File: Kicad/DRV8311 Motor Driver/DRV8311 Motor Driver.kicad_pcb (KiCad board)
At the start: 4 copper layers, 11 x 11 mm, 22 parts, among them J1 B, J2 A, J3 C, U1 DRV8311HRRWR

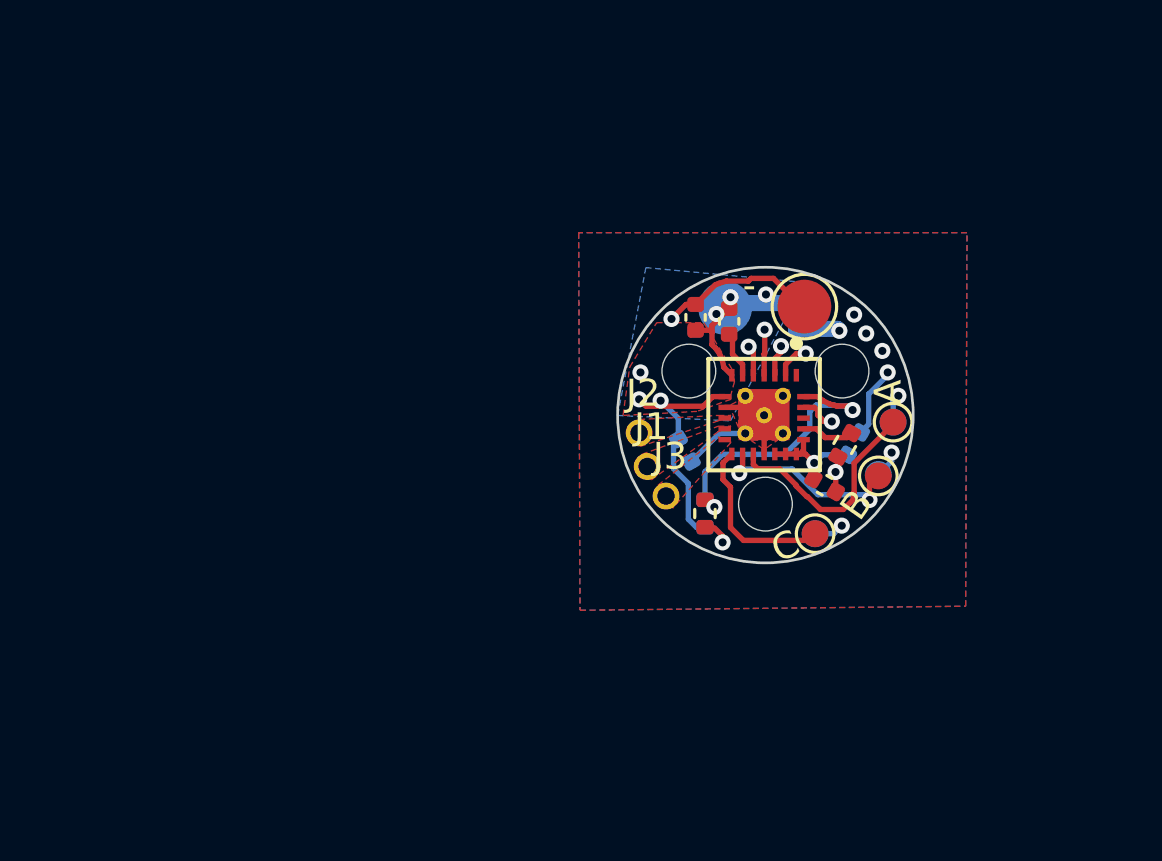
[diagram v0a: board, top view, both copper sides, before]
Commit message: Replaced external connectors
I have keystone smd low profile contacts for the power, and 1.27mm pitch headers for the data pins.
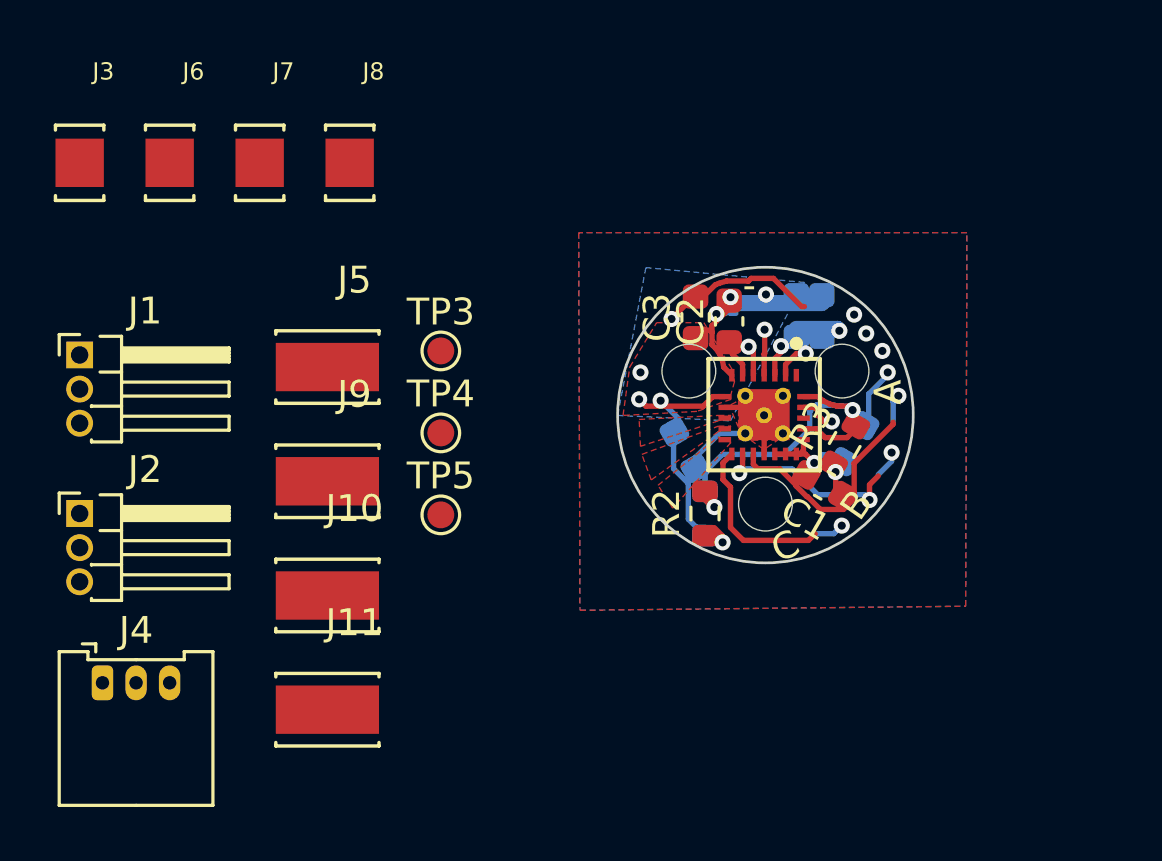
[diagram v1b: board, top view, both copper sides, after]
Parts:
- removed TP1: Power, TestPoint:TestPoint_Pad_D2.0mm
- removed TP2: GND, TestPoint:TestPoint_Pad_D2.0mm
- removed TP6: CSA-C, TestPoint:TestPoint_Pad_D1.0mm
- removed TP7: B, TestPoint:TestPoint_Pad_D1.0mm
- removed TP8: C, TestPoint:TestPoint_Pad_D1.0mm
- added J10: Keystone 6102, 6102:KEYSTONE_6102, F.Cu at (155.0, 107.2)
- added J11: Keystone 6102, 6102:KEYSTONE_6102, F.Cu at (155.0, 111.4)
- added J4: Molex Picoblade, Connector_Molex:Molex_PicoBlade_53048-0310_1x03_P1.25mm_Horizontal, F.Cu at (146.6, 110.4)
- added J5: Keystone 6102, 6102:KEYSTONE_6102, F.Cu at (155.0, 98.7)
- added J6: Keystone 6100, 6100:KEYSTONE_6100, F.Cu at (149.1, 91.0)
- added J7: Keystone 6100, 6100:KEYSTONE_6100, F.Cu at (152.5, 91.0)
- added J8: Keystone 6100, 6100:KEYSTONE_6100, F.Cu at (155.8, 91.0)
- added J9: Keystone 6102, 6102:KEYSTONE_6102, F.Cu at (155.0, 102.9)
- C1, C2, C3, C6, C7: footprint Capacitor_SMD:C_0402_1005Metric -> Capacitor_SMD:C_0603_1608Metric
- C4, C5: value 22uF -> 22uF, 16v; footprint Capacitor_SMD:C_0402_1005Metric -> Capacitor_SMD:C_0603_1608Metric
- J1: value B -> 1.27mm pin header; footprint custom_testpoints:PinHeader_1x01_P1.27mm_Round -> Connector_PinHeader_1.27mm:PinHeader_1x03_P1.27mm_Horizontal
- J2: value A -> 1.27mm pin header; footprint custom_testpoints:PinHeader_1x01_P1.27mm_Round -> Connector_PinHeader_1.27mm:PinHeader_1x03_P1.27mm_Horizontal
- J3: value C -> Keystone 6100; footprint custom_testpoints:PinHeader_1x01_P1.27mm_Round -> 6100:KEYSTONE_6100
- R1, R2, R3: footprint Resistor_SMD:R_0402_1005Metric -> Resistor_SMD:R_0603_1608Metric
- TP3: value CSA-A -> Fault; moved to F.Cu
- TP4: value CSA-B -> GND; moved to F.Cu
- TP5: value A -> 3.3v
- moved J3 25.1 mm to (145.8, 91.0)
- moved J1 21.5 mm to (145.8, 98.2)
- moved J2 21.0 mm to (145.8, 104.1)
- moved TP5 17.2 mm to (159.2, 104.2)
- moved TP4 16.4 mm to (159.2, 101.1), turned to 0 degrees
- moved TP3 15.5 mm to (159.2, 98.0), turned to 0 degrees
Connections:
- C3 pad 2: GND -> GNDPWR
- C4 pad 2: GND -> GNDPWR
- C5 pad 2: GND -> GNDPWR
- C6 pad 2: GND -> GNDPWR
- J3 pad 1: Net-(J3-Pin_1) -> GNDPWR
- TP3 pad 1: Net-(U1-SOA) -> Net-(U1-FAULT_N)
- TP4 pad 1: Net-(U1-SOB) -> GND
- TP5 pad 1: Net-(U1-INHA) -> +3.3V
- U1 pad 1: unconnected-(U1-FAULT_N-Pad1) -> Net-(U1-FAULT_N)
- U1 pad 10: Net-(J2-Pin_1) -> Net-(J4-Pin_3)
- U1 pad 11: Net-(J1-Pin_1) -> Net-(J4-Pin_2)
- U1 pad 12: Net-(J3-Pin_1) -> Net-(J4-Pin_1)
- U1 pad 13: Net-(U1-INHC) -> Net-(J2-Pin_3)
- U1 pad 14: Net-(U1-INHB) -> Net-(J2-Pin_2)
- U1 pad 15: Net-(U1-INHA) -> Net-(J2-Pin_1)
- U1 pad 25: GND -> GNDPWR
- U1 pad 3: Net-(U1-SOC) -> Net-(J1-Pin_1)
- U1 pad 4: Net-(U1-SOB) -> Net-(J1-Pin_2)
- U1 pad 5: Net-(U1-SOA) -> Net-(J1-Pin_3)
- U1 pad 9: GND -> GNDPWR
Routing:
- net (no net): track 0.00 -> 36.2 mm, vias 0 -> 2
- net Net-(U1-SOB): track 14.0 -> 0.00 mm, vias 2 -> 0
- net Net-(J1-Pin_2): track 0.00 -> 14.0 mm, vias 0 -> 2
- net Net-(U1-SOA): track 13.9 -> 0.00 mm, vias 2 -> 0
- net Net-(U1-SOC): track 13.8 -> 0.00 mm, vias 2 -> 0
- net Net-(U1-INHA): track 8.46 -> 0.00 mm
- net Net-(U1-INHB): track 7.18 -> 0.00 mm, vias 2 -> 0
- net Net-(J2-Pin_2): track 0.00 -> 7.18 mm, vias 0 -> 2
- net Net-(U1-INHC): track 6.44 -> 0.00 mm
- net Net-(J2-Pin_3): track 0.00 -> 6.44 mm
- net GND: track 17.6 -> 11.6 mm, vias 8 -> 7
- net GNDPWR: track 0.00 -> 5.97 mm, vias 0 -> 1
- net Net-(J1-Pin_1): vias 0 -> 2
- added copper zone on F.Cu, net Net-(J4-Pin_1)
- removed copper zone on F.Cu, net Net-(J3-Pin_1)

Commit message: Finished basic layout for motor driver card
The power connectors as of now have no way of contacting adjacent cards. The layout will need some tuning, but I think the components for the most part can stay in the same place.
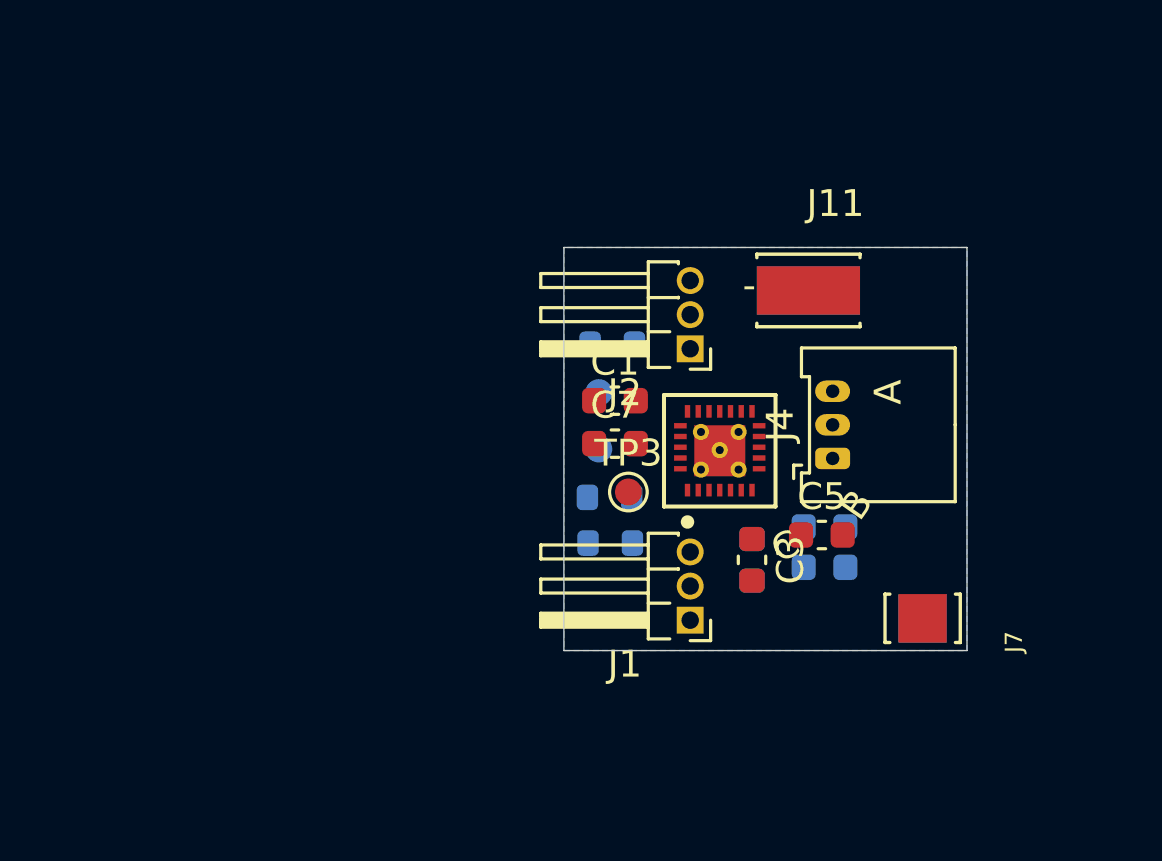
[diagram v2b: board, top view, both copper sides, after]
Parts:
- removed J10, J9: Keystone 6102, 6102:KEYSTONE_6102
- removed J6, J8: Keystone 6100, 6100:KEYSTONE_6100
- C2, J3, J5, R2, R3, TP4, TP5: moved to B.Cu
- C5, C7: moved to F.Cu
- moved J3 35.7 mm to (177.2, 108.0), turned to 90 degrees
- moved J7 29.9 mm to (177.2, 108.0), turned to -90 degrees
- moved J4 28.4 mm to (173.8, 102.0), turned to 90 degrees
- moved J1 24.8 mm to (168.5, 108.1), turned to 180 degrees
- moved J11 23.7 mm to (172.9, 95.8)
- moved J2 23.5 mm to (168.5, 98.0), turned to 180 degrees
- moved J5 18.1 mm to (172.9, 95.8), turned to 180 degrees
- moved R3 9.43 mm to (165.6, 97.8), turned to 0 degrees
- moved C3 9.27 mm to (170.8, 105.8), turned to -90 degrees
- moved C2 8.92 mm to (170.8, 105.8), turned to -90 degrees
- moved C7 8.90 mm to (165.7, 101.5), turned to 0 degrees
- moved TP3 8.73 mm to (166.2, 103.3)
- moved C1 8.41 mm to (165.7, 99.9), turned to 0 degrees
- moved C5 8.15 mm to (173.4, 104.9), turned to 0 degrees
- moved C4 7.92 mm to (173.5, 104.6), turned to 0 degrees
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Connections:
- U1 pad 10: Net-(J4-Pin_3) -> Net-(J4-Pin_1)
- U1 pad 12: Net-(J4-Pin_1) -> Net-(J4-Pin_3)
- U1 pad 3: Net-(J1-Pin_1) -> Net-(J1-Pin_3)
- U1 pad 5: Net-(J1-Pin_3) -> Net-(J1-Pin_1)
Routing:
- net (no net): track 36.2 -> 0.00 mm, vias 2 -> 0
- net VDD: track 19.0 -> 0.00 mm, vias 6 -> 0
- net Net-(J1-Pin_2): track 14.0 -> 0.00 mm, vias 2 -> 0
- net +3.3V: track 11.7 -> 0.00 mm, vias 3 -> 0
- net GND: track 11.6 -> 0.00 mm, vias 7 -> 0
- net Net-(U1-SLEEP_N): track 11.0 -> 0.00 mm, vias 2 -> 0
- net Net-(J2-Pin_2): track 7.18 -> 0.00 mm, vias 2 -> 0
- net Net-(J2-Pin_3): track 6.44 -> 0.00 mm
- net GNDPWR: track 5.97 -> 0.00 mm, vias 1 -> 0
- net Net-(U1-GAIN): track 1.99 -> 0.00 mm
- net Net-(U1-CP): track 1.73 -> 0.00 mm
- net Net-(J1-Pin_1): vias 2 -> 0
- removed copper zone on B.Cu, net GND
- removed copper zone on F.Cu, net GND
- removed copper zone on In1.Cu, net GND
- removed copper zone on F.Cu, net Net-(J1-Pin_1)
- removed copper zone on F.Cu, net Net-(J2-Pin_1)
- removed copper zone on F.Cu, net Net-(J4-Pin_1)
- removed copper zone on F.Cu, net VDD
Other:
- board size 11 x 11 mm -> 15 x 15 mm
- board text removed: "----"
- board text removed: "08/17/2024"
- board text removed: "1"
- board text removed: "1 of 1"
- board text removed: "2"
- board text removed: "8:1"
- board text removed: "APPROVED"
- board text removed: "ASHER"
- board text removed: "BREAK ALL SHARP EDGES AND REMOVE BURRS"
- board text removed: "Bottom Motor view"
- board text removed: "CHECKED"
- board text removed: "DATE"
- board text removed: "DO NOT SCALE DRAWING"
- board text removed: "DRAWN"
- board text removed: "DWG NO."
- board text removed: "FINISH"
- board text removed: "MATERIAL"
- board text removed: "NAME"
- board text removed: "REV."
- board text removed: "SCALE"
- board text removed: "SHEET"
- board text removed: "SIZE"
- board text removed: "SURFACE FINISH"
- board text removed: "THIRD ANGLE PROJECTION"
- board text removed: "TITLE"
- board text removed: "UNLESS OTHERWISE SPECIFIED, DIMENSIONS ARE IN MILLIMETERS"
- board text removed: "WEIGHT"

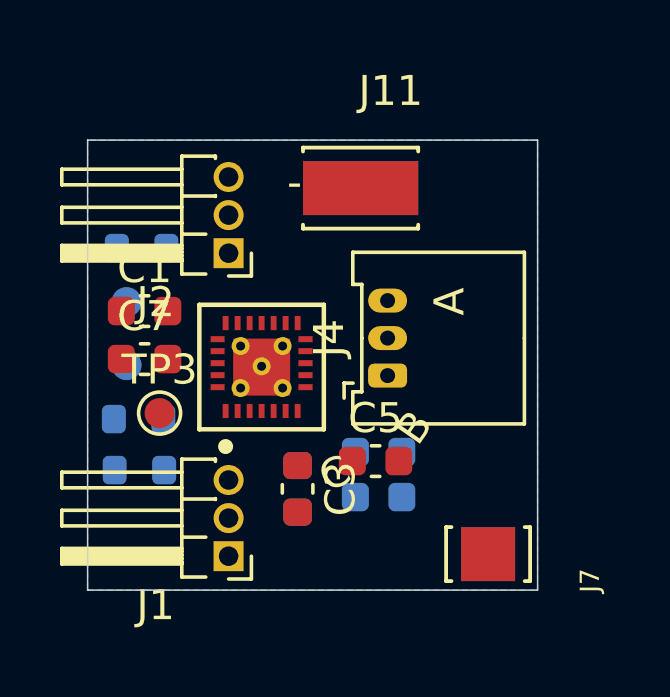
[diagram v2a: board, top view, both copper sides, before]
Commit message: Re-arranged components for better mating
The power connectors now should make contact. The difficulty will be getting them in, because they are supposed to go forward and I'm causing the connectors to slide in sidewards.
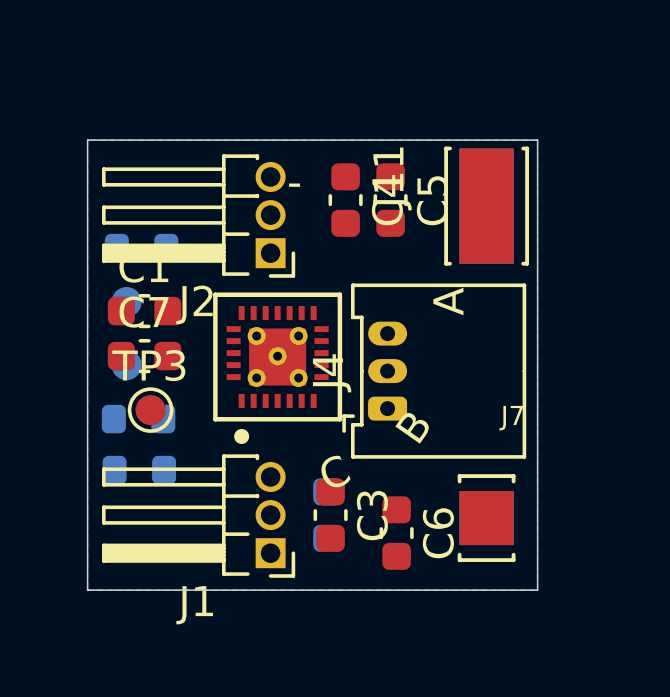
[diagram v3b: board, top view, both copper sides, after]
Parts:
- C4, C6: moved to F.Cu
- moved C5 8.71 mm to (173.9, 96.2), turned to -90 degrees
- moved C4 8.47 mm to (172.4, 96.2), turned to -90 degrees
- moved J11 4.24 mm to (177.1, 96.4), turned to 90 degrees
- moved J5 4.24 mm to (177.1, 96.4), turned to -90 degrees
- moved C3 1.41 mm to (171.9, 106.7)
- moved J1 1.40 mm to (169.9, 108.0)
- moved J2 1.40 mm to (169.9, 98.0)
- moved C6 1.34 mm to (174.1, 107.3), turned to -90 degrees
- moved C2 1.33 mm to (171.8, 106.7)
- moved J3 1.20 mm to (177.1, 106.8), turned to 180 degrees
- moved J7 1.20 mm to (177.1, 106.8), turned to 0 degrees
- moved J4 1.10 mm to (173.8, 103.2)
- moved U1 0.63 mm to (170.1, 101.4)
- moved TP3 0.32 mm to (165.9, 103.2)
- moved C7 0.10 mm to (165.7, 101.4)

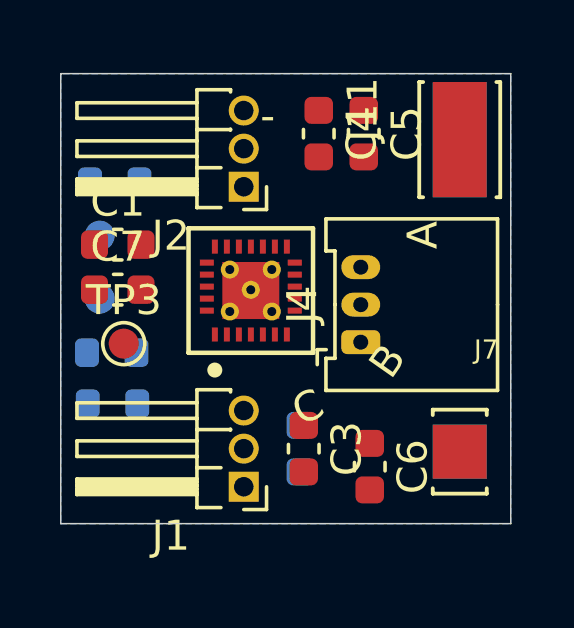
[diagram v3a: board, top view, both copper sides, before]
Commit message: Finished basic routing
I still need to optimize it, and work out how to improve conductivity and thermal properties
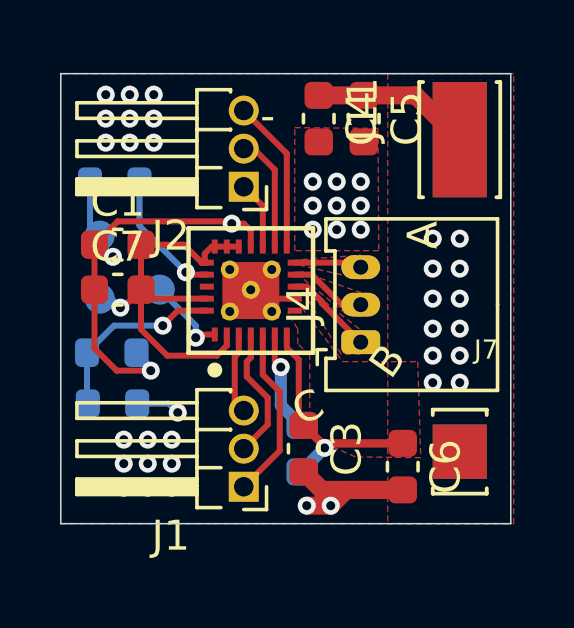
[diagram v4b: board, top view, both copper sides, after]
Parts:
- TP3: moved to B.Cu
- moved TP3 2.16 mm to (167.1, 101.4), turned to 180 degrees
- moved C6 1.10 mm to (175.2, 107.3)
- moved C4 0.50 mm to (172.4, 95.7)
- moved C5 0.50 mm to (173.9, 95.7)
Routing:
- net VDD: track 0.00 -> 21.0 mm, vias 0 -> 14
- net GND: track 0.00 -> 16.2 mm, vias 0 -> 3
- net +3.3V: track 0.00 -> 14.6 mm, vias 0 -> 1
- net GNDPWR: track 0.00 -> 8.54 mm, vias 0 -> 29
- net Net-(U1-SLEEP_N): track 0.00 -> 6.29 mm, vias 0 -> 1
- net Net-(J1-Pin_1): track 0.00 -> 5.81 mm
- net Net-(J2-Pin_3): track 0.00 -> 5.13 mm
- net Net-(J1-Pin_2): track 0.00 -> 4.48 mm
- net Net-(U1-GAIN): track 0.00 -> 4.29 mm, vias 0 -> 1
- net Net-(J2-Pin_2): track 0.00 -> 3.89 mm
- net Net-(U1-CP): track 0.00 -> 3.39 mm, vias 0 -> 1
- net Net-(J4-Pin_1): track 0.00 -> 3.00 mm
- net Net-(U1-FAULT_N): track 0.00 -> 2.78 mm, vias 0 -> 1
- net Net-(J1-Pin_3): track 0.00 -> 2.72 mm
- net Net-(J4-Pin_2): track 0.00 -> 2.61 mm
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- added copper zone on B.Cu, net GNDPWR
- added copper zone on F.Cu, net GNDPWR
- added copper zone on In2.Cu, net GNDPWR
- added copper zone on F.Cu, net Net-(J4-Pin_1)
- added copper zone on F.Cu, net Net-(J4-Pin_2)
- added copper zone on F.Cu, net Net-(J4-Pin_3)
- added copper zone on F.Cu, net VDD
- added copper zone on In1.Cu, net VDD
- removed copper zone on B.Cu, net VDD
- removed copper zone on In2.Cu, net VDD

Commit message: Finished silkscreen, adjusted component placements and vias
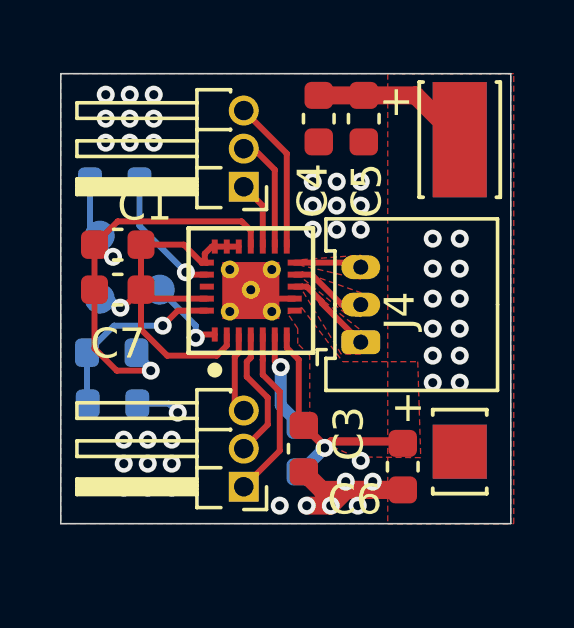
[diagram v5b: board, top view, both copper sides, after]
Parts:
- turned J5 to 90 degrees
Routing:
- net GND: vias 3 -> 2
- net GNDPWR: vias 29 -> 34
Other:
- board text added: "C B A"
- board text added: "CSA"
- board text added: "PWM"
- board text removed: "A"
- board text removed: "B"
- board text removed: "C"
